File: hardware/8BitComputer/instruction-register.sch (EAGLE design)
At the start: 51 parts, among them IC1 SN74LS173ANG4, IC2 SN74LS173ANG4, IC3 SN74LS245NE4, IC4 SN74LS173ANG4, IC5 SN74LS173ANG4, IC6 SN74LS245NE4, J1 BUS OUT, J2 pwr, J4 BUS OUT

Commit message: 3 registers and an instruction register complete
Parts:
- LED13, LED14, LED15, LED16: value red -> blue
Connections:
- net R1_173_CLR renamed IR_173_CLR
- net R1_173_LOAD renamed IR_173_LOAD
- net R1_173_OUT_B0 renamed IR_173_OUT_B0
- net R1_173_OUT_B1 renamed IR_173_OUT_B1
- net R1_173_OUT_B2 renamed IR_173_OUT_B2
- net R1_173_OUT_B3 renamed IR_173_OUT_B3
- net R1_245_DIR renamed IR_245_DIR
- net R1_245_OUTPUT_ENABLE renamed IR_245_OUTPUT_ENABLE
- net R1_BUS0 renamed IR_BUS0
- net R1_BUS1 renamed IR_BUS1
- net R1_BUS2 renamed IR_BUS2
- net R1_BUS3 renamed IR_BUS3
- net R1_BUS4 renamed IR_BUS4
- net R1_BUS5 renamed IR_BUS5
- net R1_BUS6 renamed IR_BUS6
- net R1_BUS7 renamed IR_BUS7
- net R2_173_CLR renamed R3_173_CLR
- net R2_173_LOAD renamed R3_173_LOAD
- net R2_173_OUT_B0 renamed R3_173_OUT_B0
- net R2_173_OUT_B1 renamed R3_173_OUT_B1
- net R2_173_OUT_B2 renamed R3_173_OUT_B2
- net R2_173_OUT_B3 renamed R3_173_OUT_B3
- net R2_173_OUT_B4 renamed R3_173_OUT_B4
- net R2_173_OUT_B5 renamed R3_173_OUT_B5
- net R2_173_OUT_B6 renamed R3_173_OUT_B6
- net R2_173_OUT_B7 renamed R3_173_OUT_B7
- net R2_245_DIR renamed R3_245_DIR
- net R2_245_OUTPUT_ENABLE renamed R3_245_OUTPUT_ENABLE
- net R2_BUS0 renamed R3_BUS0
- net R2_BUS1 renamed R3_BUS1
- net R2_BUS2 renamed R3_BUS2
- net R2_BUS3 renamed R3_BUS3
- net R2_BUS4 renamed R3_BUS4
- net R2_BUS5 renamed R3_BUS5
- net R2_BUS6 renamed R3_BUS6
- net R2_BUS7 renamed R3_BUS7
- removed net R1_173_OUT_B4: IC5.1Q, IC6.A4, LED13.A
- removed net R1_173_OUT_B5: IC5.2Q, IC6.A3, LED14.A
- removed net R1_173_OUT_B6: IC5.3Q, IC6.A2, LED15.A
- removed net R1_173_OUT_B7: IC5.4Q, IC6.A1, LED16.A
- new net IR_4: IC5.1Q, LED13.A
- new net IR_5: IC5.2Q, LED14.A
- new net IR_6: IC5.3Q, LED15.A
- new net IR_7: IC5.4Q, LED16.A
- net GND: now also IC6.A1, IC6.A2, IC6.A3, IC6.A4

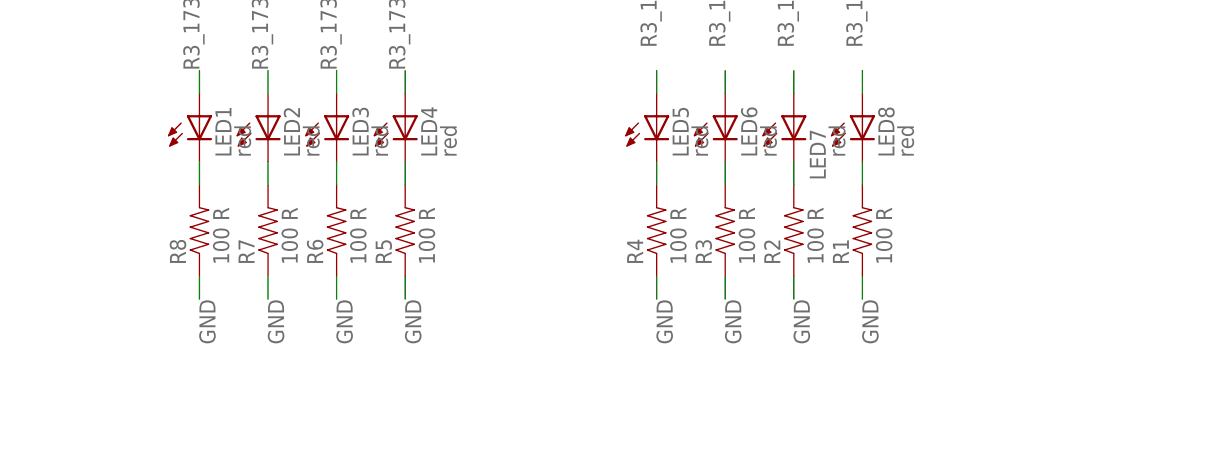
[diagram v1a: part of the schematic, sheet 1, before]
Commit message: adding static ram chip updated all other boards to remove led resistors that aren't needed
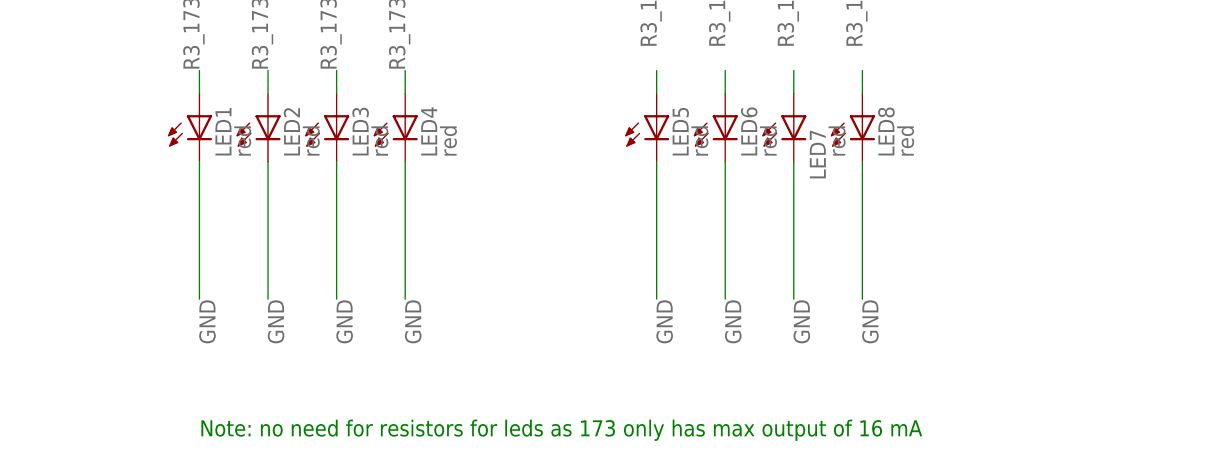
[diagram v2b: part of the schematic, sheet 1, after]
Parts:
- removed R1, R10, R11, R12, R13, R14, R15, R16, R2, R3, R4, R5, R6, R7, R8, R9: 100 R, passives:RESISTOR0805-RES
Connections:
- removed net N$1: LED9.C, R16.2
- removed net N$2: LED10.C, R15.2
- removed net N$27: LED1.C, R8.2
- removed net N$28: LED2.C, R7.2
- removed net N$29: LED3.C, R6.2
- removed net N$3: LED11.C, R14.2
- removed net N$30: LED4.C, R5.2
- removed net N$31: LED5.C, R4.2
- removed net N$32: LED6.C, R3.2
- removed net N$33: LED7.C, R2.2
- removed net N$34: LED8.C, R1.2
- removed net N$4: LED12.C, R13.2
- removed net N$5: LED13.C, R12.2
- removed net N$6: LED14.C, R11.2
- removed net N$7: LED15.C, R10.2
- removed net N$8: LED16.C, R9.2
- net GND: now also LED1.C, LED10.C, LED11.C, LED12.C, LED13.C, LED14.C, LED15.C, LED16.C, LED2.C, LED3.C, LED4.C, LED5.C, LED6.C, LED7.C, LED8.C, LED9.C; no longer R1.1, R10.1, R11.1, R12.1, R13.1, R14.1, R15.1, R16.1, R2.1, R3.1, R4.1, R5.1, R6.1, R7.1, R8.1, R9.1
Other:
- note added: "Note: no need for resistors for leds as 173 only has max output of 16 mA"
